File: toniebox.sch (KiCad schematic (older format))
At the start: 109 parts, among them K4 Conn_01x03, K9 Conn_01x03, T11 Q_NMOS_GSD, T4 Q_NMOS_GSD, T5 Q_NMOS_GSD, T6 Q_NMOS_GSD, T7 Q_NMOS_GSD, U2 CC3200

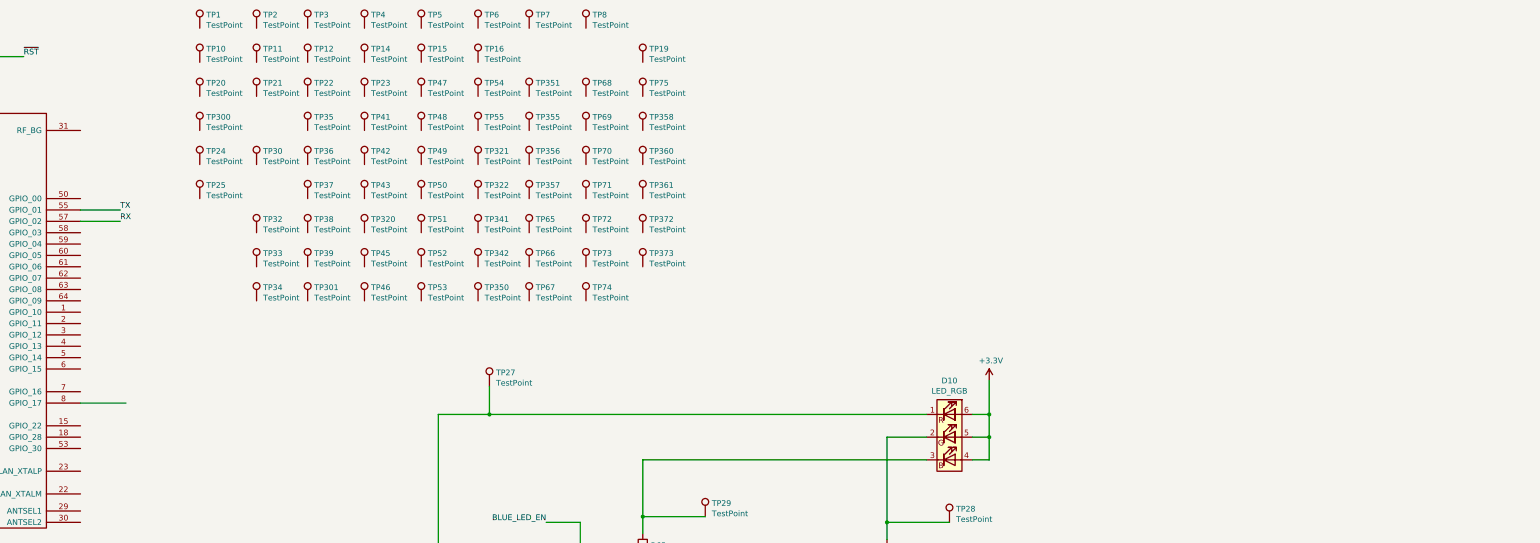
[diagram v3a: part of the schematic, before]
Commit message: testpoints, LDOs
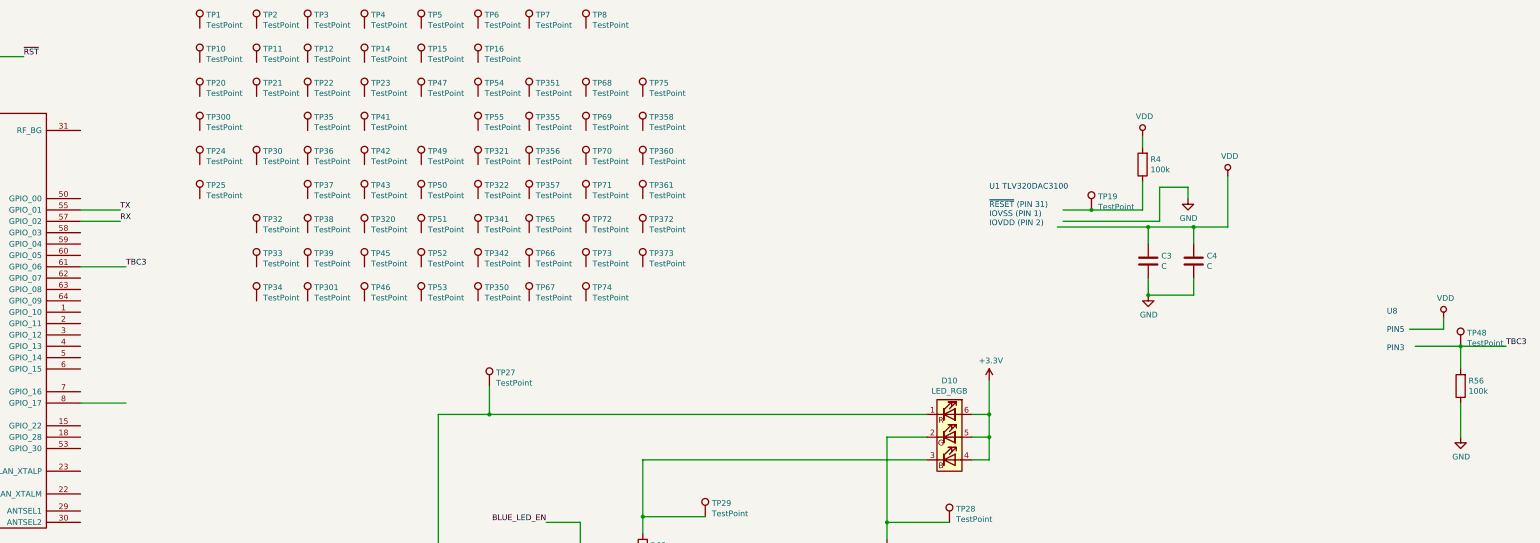
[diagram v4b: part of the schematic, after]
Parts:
- added C3, C4: C, symbol Device:C
- added R4, R56: 100k, symbol Device:R
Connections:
- net labels added: TBC3
- wire segments 115 -> 139
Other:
- note added: "U1 TLV320DAC3100\n\n~RESET~ (PIN 31)\nIOVSS (PIN 1)\nIOVDD (PIN 2)"
- note added: "U8 \n\nPIN5\n\nPIN3"
- moved on the sheet: TP19, TP48
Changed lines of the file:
@@
 EELAYER 30 0
 EELAYER END
-$Descr A3 16535 11693
+$Descr A2 23386 16535
 encoding utf-8
 Sheet 1 1
@@
 L Connector:TestPoint TP48
 U 1 1 5E31177E
-P 8450 1900
-F 0 "TP48" H 8508 2018 50  0000 L CNN
-F 1 "TestPoint" H 8508 1927 50  0000 L CNN
-F 2 "" H 8650 1900 50  0001 C CNN
-F 3 "~" H 8650 1900 50  0001 C CNN
-	1    8450 1900
+P 17600 3800
+F 0 "TP48" H 17658 3918 50  0000 L CNN
+F 1 "TestPoint" H 17658 3827 50  0000 L CNN
+F 2 "" H 17800 3800 50  0001 C CNN
+F 3 "~" H 17800 3800 50  0001 C CNN
+	1    17600 3800
 	1    0    0    -1
 $EndComp
@@
 L Connector:TestPoint TP19
 U 1 1 5E30EBD1
-P 10400 1300
-F 0 "TP19" H 10458 1418 50  0000 L CNN
-F 1 "TestPoint" H 10458 1327 50  0000 L CNN
-F 2 "" H 10600 1300 50  0001 C CNN
-F 3 "~" H 10600 1300 50  0001 C CNN
-	1    10400 1300
+P 14350 2600
+F 0 "TP19" H 14408 2718 50  0000 L CNN
+F 1 "TestPoint" H 14408 2627 50  0000 L CNN
+F 2 "" H 14550 2600 50  0001 C CNN
+F 3 "~" H 14550 2600 50  0001 C CNN
+	1    14350 2600
 	1    0    0    -1
 $EndComp
@@
 Wire Wire Line
 	9600 8550 9600 8600
+$Comp
+L power:VDD #PWR?
+U 1 1 5E40199F
+P 14800 1950
+F 0 "#PWR?" H 14800 1800 50  0001 C CNN
+F 1 "VDD" H 14817 2123 50  0000 C CNN
+F 2 "" H 14800 1950 50  0001 C CNN
+F 3 "" H 14800 1950 50  0001 C CNN
+	1    14800 1950
+	1    0    0    -1
+$EndComp
+$Comp
+L Device:R R4
+U 1 1 5E402CAD
+P 14800 2200
+F 0 "R4" H 14730 2154 50  0000 R CNN
+F 1 "100k" H 14730 2245 50  0000 R CNN
+F 2 "" V 14730 2200 50  0001 C CNN
+F 3 "~" H 14800 2200 50  0001 C CNN
+	1    14800 2200
+	-1   0    0    1
+$EndComp
+Text Notes 13450 2750 0    50   ~ 0
+U1 TLV320DAC3100\n\n~RESET~ (PIN 31)\nIOVSS (PIN 1)\nIOVDD (PIN 2)
+Wire Wire Line
+	14800 2050 14800 1950
+Wire Wire Line
+	14800 2350 14800 2600
+Wire Wire Line
+	14800 2600 14350 2600
+Connection ~ 14350 2600
+Wire Wire Line
+	14350 2600 14100 2600
+Wire Wire Line
+	5450 3100 5850 3100
+Text Label 5850 3100 0    50   ~ 0
+TBC3
+Wire Wire Line
+	17600 3800 18000 3800
+Text Label 18000 3800 0    50   ~ 0
+TBC3
+Text Notes 16950 3850 0    50   ~ 0
+U8 \n\nPIN5\n\nPIN3
+Wire Wire Line
+	17600 3800 17200 3800
+Connection ~ 17600 3800
+$Comp
+L Device:R R56
+U 1 1 5E41E049
+P 17600 4150
+F 0 "R56" H 17530 4104 50  0000 R CNN
+F 1 "100k" H 17530 4195 50  0000 R CNN
+F 2 "" V 17530 4150 50  0001 C CNN
+F 3 "~" H 17600 4150 50  0001 C CNN
+	1    17600 4150
+	-1   0    0    1
+$EndComp
+Wire Wire Line
+	17600 3800 17600 4000
+Wire Wire Line
+	17600 4300 17600 4600
+$Comp
+L power:GND #PWR?
+U 1 1 5E42683A
+P 17600 4600
+F 0 "#PWR?" H 17600 4350 50  0001 C CNN
+F 1 "GND" H 17605 4427 50  0000 C CNN
+F 2 "" H 17600 4600 50  0001 C CNN
+F 3 "" H 17600 4600 50  0001 C CNN
+	1    17600 4600
+	1    0    0    -1
+$EndComp
+Wire Wire Line
+	15550 2750 15550 2300
+$Comp
+L power:VDD #PWR?
+U 1 1 5E42B88F
+P 15550 2300
+F 0 "#PWR?" H 15550 2150 50  0001 C CNN
+F 1 "VDD" H 15567 2473 50  0000 C CNN
+F 2 "" H 15550 2300 50  0001 C CNN
+F 3 "" H 15550 2300 50  0001 C CNN
+	1    15550 2300
+	1    0    0    -1
+$EndComp
+Wire Wire Line
+	14100 2700 14950 2700
+$Comp
+L power:GND #PWR?
+U 1 1 5E4305F0
+P 15200 2500
+F 0 "#PWR?" H 15200 2250 50  0001 C CNN
+F 1 "GND" H 15205 2327 50  0000 C CNN
+F 2 "" H 15200 2500 50  0001 C CNN
+F 3 "" H 15200 2500 50  0001 C CNN
+	1    15200 2500
+	1    0    0    -1
+$EndComp
+Wire Wire Line
+	14950 2400 15200 2400
+Wire Wire Line
+	15200 2400 15200 2500
+Wire Wire Line
+	14950 2400 14950 2700
+Wire Wire Line
+	14050 2750 14850 2750
+$Comp
+L Device:C C3
+U 1 1 5E43BABF
+P 14850 3050
+F 0 "C3" H 14965 3096 50  0000 L CNN
+F 1 "C" H 14965 3005 50  0000 L CNN
+F 2 "" H 14888 2900 50  0001 C CNN
+F 3 "~" H 14850 3050 50  0001 C CNN
+	1    14850 3050
+	1    0    0    -1
+$EndComp
+$Comp
+L Device:C C4
+U 1 1 5E43BD4F
+P 15250 3050
+F 0 "C4" H 15365 3096 50  0000 L CNN
+F 1 "C" H 15365 3005 50  0000 L CNN
+F 2 "" H 15288 2900 50  0001 C CNN
+F 3 "~" H 15250 3050 50  0001 C CNN
+	1    15250 3050
+	1    0    0    -1
+$EndComp
+Wire Wire Line
+	14850 2750 14850 2900
+Connection ~ 14850 2750
+Wire Wire Line
+	14850 2750 15250 2750
+Wire Wire Line
+	15250 2750 15250 2900
+Connection ~ 15250 2750
+Wire Wire Line
+	15250 2750 15550 2750
+Wire Wire Line
+	14850 3200 14850 3350
+Wire Wire Line
+	14850 3350 15250 3350
+Wire Wire Line
+	15250 3350 15250 3200
+$Comp
+L power:GND #PWR?
+U 1 1 5E44A408
+P 14850 3350
+F 0 "#PWR?" H 14850 3100 50  0001 C CNN
+F 1 "GND" H 14855 3177 50  0000 C CNN
+F 2 "" H 14850 3350 50  0001 C CNN
+F 3 "" H 14850 3350 50  0001 C CNN
+	1    14850 3350
+	1    0    0    -1
+$EndComp
+Connection ~ 14850 3350
+Wire Wire Line
+	17150 3650 17450 3650
+Wire Wire Line
+	17450 3650 17450 3550
+$Comp
+L power:VDD #PWR?
+U 1 1 5E45450E
+P 17450 3550
+F 0 "#PWR?" H 17450 3400 50  0001 C CNN
+F 1 "VDD" H 17467 3723 50  0000 C CNN
+F 2 "" H 17450 3550 50  0001 C CNN
+F 3 "" H 17450 3550 50  0001 C CNN
+	1    17450 3550
+	1    0    0    -1
+$EndComp
 $EndSCHEMATC

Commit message: add datasheet, progress images, library
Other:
- note added: "U8 AP2112K-3.3TRG1?\n\nPIN5\n\nPIN3"
- note added: "U9 AP2120N-1.8TRG1?\n"
- note removed: "U8 \n\nPIN5\n\nPIN3"
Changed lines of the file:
@@
 TBC3
 Text Notes 16950 3850 0    50   ~ 0
-U8 \n\nPIN5\n\nPIN3
+U8 AP2112K-3.3TRG1?\n\nPIN5\n\nPIN3
 Wire Wire Line
 	17600 3800 17200 3800
@@
 	1    0    0    -1
 $EndComp
+Text Notes 16900 2700 0    50   ~ 0
+U9 AP2120N-1.8TRG1?\n
 $EndSCHEMATC

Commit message: add mosfet datasheet, more ICs
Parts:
- removed T11, T4, T5, T6, T7: Q_NMOS_GSD, symbol Device:Q_NMOS_GSD
- removed U2: CC3200, symbol CC3200:CC3200
- added T11: FDV301N, Package_TO_SOT_SMD:SOT-23, symbol dk_Transistors-FETs-MOSFETs-Single:FDV301N
- added T4, T5, T6, T7: FDV301N, digikey-footprints:SOT-23-3, symbol dk_Transistors-FETs-MOSFETs-Single:FDV301N
- added U1: TLV320DAC3100, Package_DFN_QFN:Texas_S-PVQFN-N32_EP3.45x3.45mm, symbol toniebox:TLV320DAC3100
- added U2: CC3200R1M2RGCR, digikey-footprints:VFQFN-64-1EP_9x9mm, symbol dk_RF-Transceiver-ICs:CC3200R1M2RGCR
- added U3: IS25LQ032B-JNLE, Package_SO:TSSOP-8_4.4x3mm_P0.65mm, symbol toniebox:IS25LQ032B-JNLE
- added U4: MMA8451QT, digikey-footprints:VQFN-16_3x3mm, symbol dk_Motion-Sensors-Accelerometers:MMA8451QT
- added U8: AP2112K-3.3, Package_TO_SOT_SMD:SOT-23-5, symbol Regulator_Linear:AP2112K-3.3
- added U9: AP2120N-1.8, Package_TO_SOT_SMD:SOT-23, symbol toniebox:AP2120N-1.8
- gave numbers to parts that had none: 4
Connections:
- wire segments 139 -> 138
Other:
- note removed: "U1 TLV320DAC3100\n\n~RESET~ (PIN 31)\nIOVSS (PIN 1)\nIOVDD (PIN 2)"
- note removed: "U3 IS25LQ032B\n\nWP#/IO2\nHOLD#/IO3\n\nSO/IO2 (PIN 2)"
- note removed: "U4 MMA8451Q\n\nVDDIO (PIN 1)"
- note removed: "U8 AP2112K-3.3TRG1?\n\nPIN5\n\nPIN3"
- note removed: "U9 AP2120N-1.8TRG1?\n"
- moved on the sheet: C3, C4, R11, R4, R56, R?1, TP19, TP370, TP48, TP9

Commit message: sd card
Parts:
- added K2: Micro_SD_Card_Det_Hirose_DM3CS, symbol toniebox:Micro_SD_Card_Det_Hirose_DM3CS
- added R17, R18, R19, R20, R21: 10k, symbol Device:R
- added R22, R360: N/A, symbol Device:R
- added R73, R74: 2k7, symbol Device:R
- added T360: FDV301N, Package_TO_SOT_SMD:SOT-23, symbol dk_Transistors-FETs-MOSFETs-Single:FDV301N
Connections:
- net GND: now also K2.10 (SHIELD), K2.11 (SHIELD), K2.12 (SHIELD), K2.13 (SHIELD), K2.6 (VSS)
- net VDD: now also R73.1, R74.1
- net at TP3.1: now also K2.9 (DETECT), R22.2
- net I2C_SDA: now reaches TP351.1
- net I2C_SDA: now also U1.9 (SDA), U2.4 (GPIO13), U4.6 (SDA), R73.2
- net VCC: now reaches TP360.1
- net VCC: now also K2.4 (VDD), R17.1, R18.1, R19.1, R20.1, R21.1, R22.1, T360.3 (D)
- net I2C_SCL: now reaches TP350.1
- net I2C_SCL: now also U1.10 (SCL), U2.3 (GPIO12), U4.4 (SCL), R74.2
- net SD_CLK: now reaches U2.1 (GPIO10)
- net SD_CLK: now also K2.5 (CLK)
- net SD_CMD: now reaches U2.2 (GPIO11)
- net SD_CMD: now also K2.3 (CMD), R19.2
- net SD_DAT0: now reaches U2.64 (GPIO9)
- net SD_DAT0: now also K2.7 (DAT0), R20.2
- new net: K2.1 (DAT2), R17.2
- new net: K2.2 (DAT3/CD), R18.2
- new net: K2.8 (DAT1), R21.2
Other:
- note added: "?"
- note added: "R17-22, K2, R73, R74, T360\nTP351, TP350, TP360, TP3"
- note added: "SD VDD -> ?"
- moved on the sheet: R4, TP3, TP350, TP351, TP360, TP9, U3, U9
